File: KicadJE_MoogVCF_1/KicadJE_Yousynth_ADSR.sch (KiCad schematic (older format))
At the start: 52 parts, among them J301 ADSRGate, J302 ADSR, P301 Doepfer_Power_10pin, Q301 SI2302, Q302 MMBT3904, Q303 MMBT3904, Q304 MMBT3904, SW301 SW_DPDT_x2, SW302 Gate, U301 TL072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

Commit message: ERC done
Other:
- moved on the sheet: C301, C302, C303, C304, D301, D302, U301C

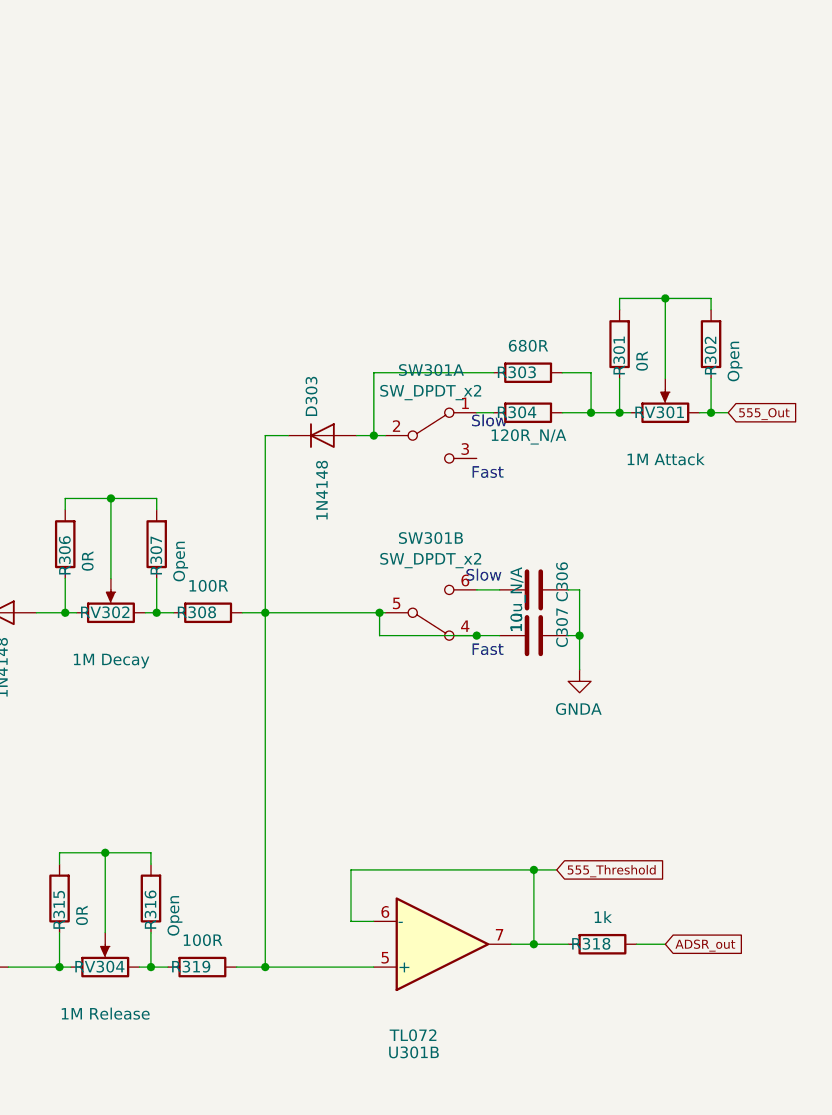
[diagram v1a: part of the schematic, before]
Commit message: Review R-Open names after initial assembley - ADSR
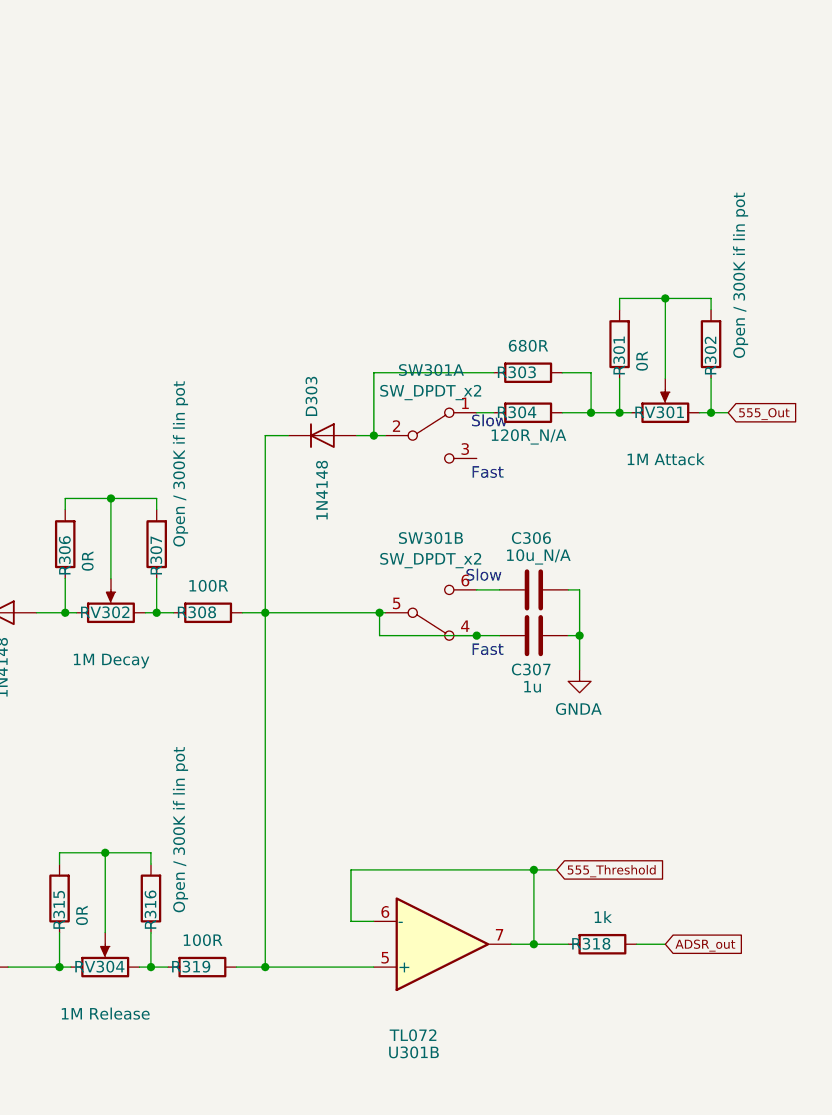
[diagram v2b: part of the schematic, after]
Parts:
- R302, R307, R316: value Open -> Open / 300K if lin pot
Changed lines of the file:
@@
 EESchema Schematic File Version 4
+LIBS:KicadJE_MoogVCF_1-cache
 EELAYER 29 0
 EELAYER END
@@
 AR Path="/5F18E4B5/5F304EF5" Ref="R307"  Part="1"
 F 0 "R307" V 6225 2925 50  0000 C CNN
-F 1 "Open" V 6125 2950 50  0000 C CNN
+F 1 "Open / 300K if lin pot" V 6125 2525 50  0000 C CNN
 F 2 "Resistor_SMD:R_0805_2012Metric_Pad1.15x1.40mm_HandSolder" V 6155 2875 50  0001 C CNN
 F 3 "~" H 6225 2875 50  0001 C CNN
@@
 AR Path="/5F18E4B5/5F307F53" Ref="R316"  Part="1"
 F 0 "R316" V 6200 4475 50  0000 C CNN
-F 1 "Open" V 6100 4500 50  0000 C CNN
+F 1 "Open / 300K if lin pot" V 6075 4125 50  0000 C CNN
 F 2 "Resistor_SMD:R_0805_2012Metric_Pad1.15x1.40mm_HandSolder" V 6130 4425 50  0001 C CNN
 F 3 "~" H 6200 4425 50  0001 C CNN
@@
 AR Path="/5F18E4B5/5F30DFD9" Ref="R302"  Part="1"
 F 0 "R302" V 8650 2050 50  0000 C CNN
-F 1 "Open" V 8550 2075 50  0000 C CNN
+F 1 "Open / 300K if lin pot" V 8525 1700 50  0000 C CNN
 F 2 "Resistor_SMD:R_0805_2012Metric_Pad1.15x1.40mm_HandSolder" V 8580 2000 50  0001 C CNN
 F 3 "~" H 8650 2000 50  0001 C CNN
@@
 AR Path="/5DD87D87/5F341D70" Ref="C?"  Part="1"
 AR Path="/5F18E4B5/5F341D70" Ref="C306"  Part="1"
-F 0 "C306" H 7750 3200 50  0000 L CNN
-F 1 "10u_N/A" H 7775 3000 50  0000 L CNN
+F 0 "C306" V 7650 2975 50  0000 L CNN
+F 1 "10u_N/A" V 7725 2950 50  0000 L CNN
 F 2 "Capacitor_SMD:C_0805_2012Metric_Pad1.15x1.40mm_HandSolder" H 7913 2925 50  0001 C CNN
 F 3 "~" H 7875 3075 50  0001 C CNN
@@
 AR Path="/5DD87D87/5F342595" Ref="C?"  Part="1"
 AR Path="/5F18E4B5/5F342595" Ref="C307"  Part="1"
-F 0 "C307" H 7750 3400 50  0000 L CNN
-F 1 "1u" H 7775 3200 50  0000 L CNN
+F 0 "C307" V 8025 3175 50  0000 L CNN
+F 1 "1u" V 8100 3225 50  0000 L CNN
 F 2 "Capacitor_SMD:C_0805_2012Metric_Pad1.15x1.40mm_HandSolder" H 7913 3125 50  0001 C CNN
 F 3 "~" H 7875 3275 50  0001 C CNN
